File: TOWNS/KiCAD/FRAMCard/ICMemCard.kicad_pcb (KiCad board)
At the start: 2 copper layers, 79.1 x 50.5 mm, 18 parts, among them J1 PCMCIA_Connector, Q1 BC846X, Q2 BC846X, U1 FM18W08-SGTR, U2 FM18W08-SGTR

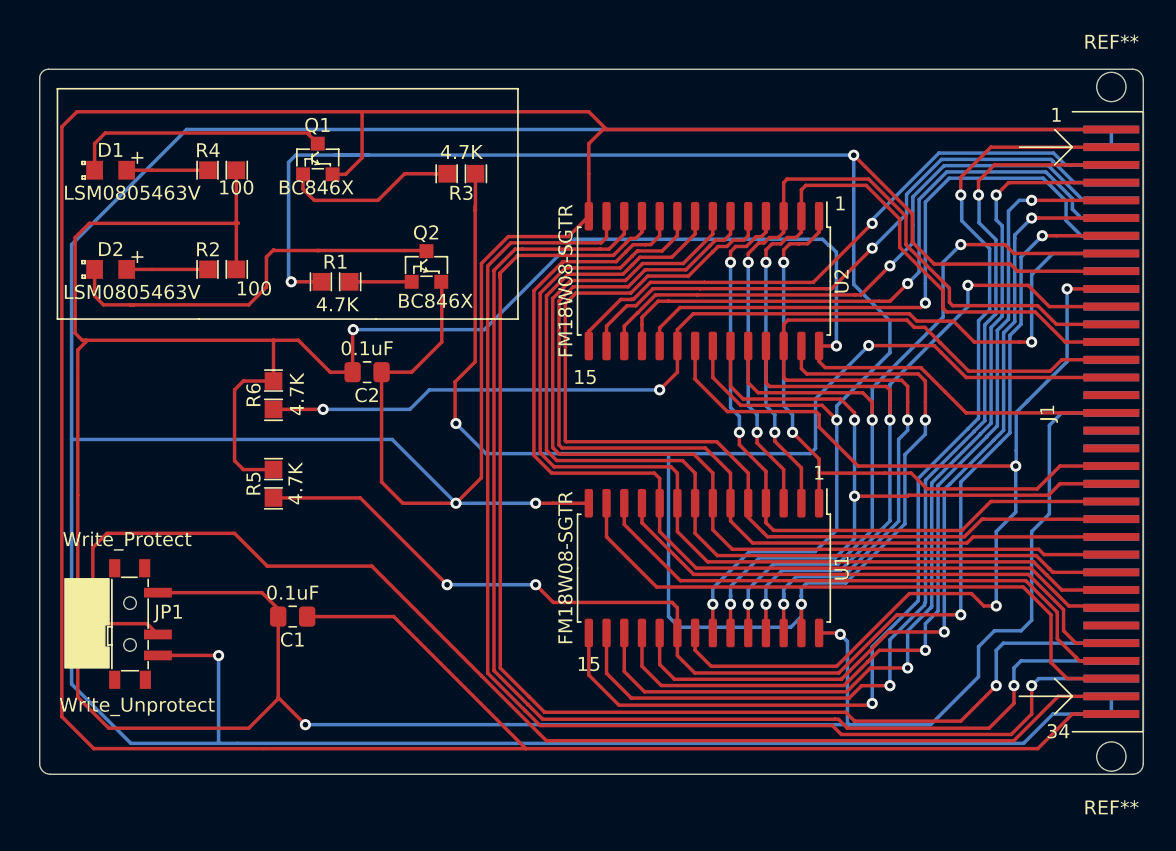
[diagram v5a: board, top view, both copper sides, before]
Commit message: Added OR-gate to enforce Write Protection.
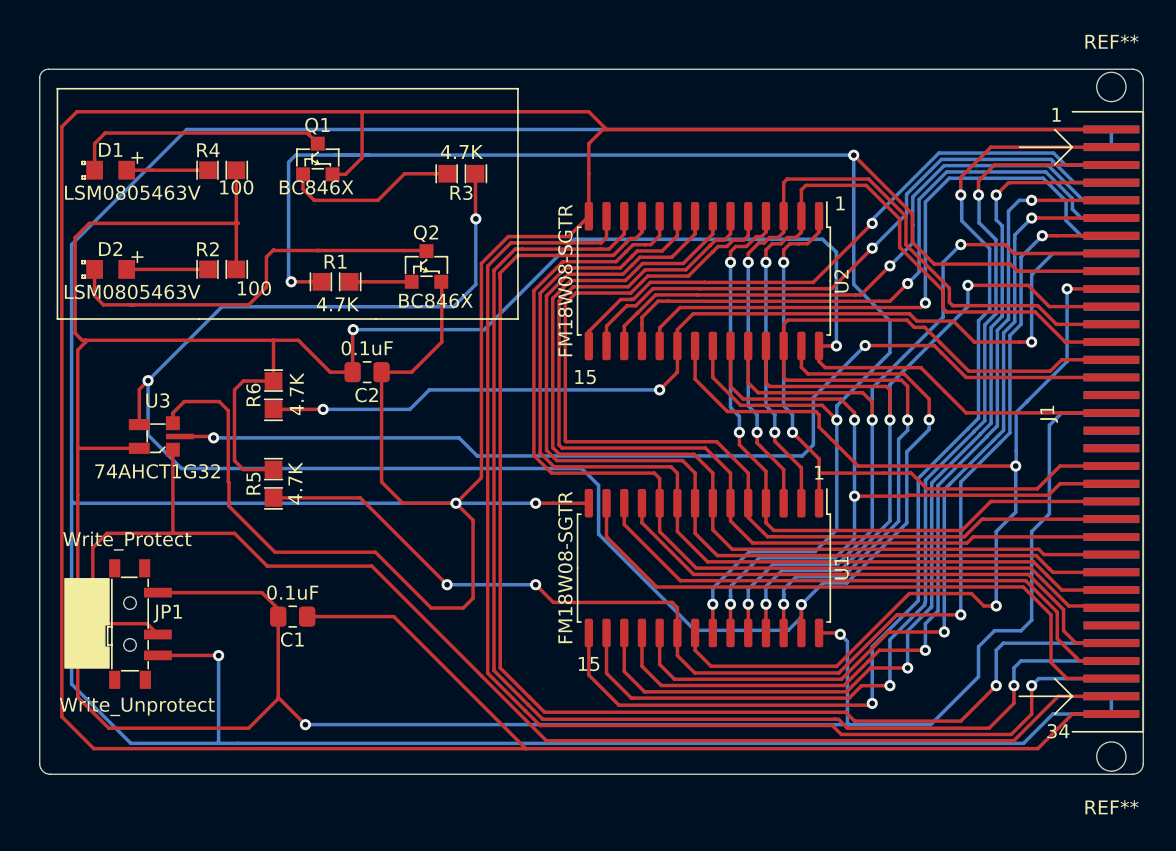
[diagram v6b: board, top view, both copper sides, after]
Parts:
- added U3: 74AHCT1G32, PCMCIA:SOT353_Easy, F.Cu at (70.7, 77.0)
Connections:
- R3 pad 2: /~WE -> /~WE~orWP
- U1 pad 27: /~WE -> /~WE~orWP
- U2 pad 27: /~WE -> /~WE~orWP
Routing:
- net /~WE~orWP: track 0.00 -> 130.8 mm, vias 0 -> 4
- net /~WE: track 130.4 -> 73.6 mm, vias 4 -> 2
- net GND: track 517.5 -> 555.9 mm
- net /Wp: track 90.8 -> 96.8 mm
- net Vcc: track 278.0 -> 282.4 mm
